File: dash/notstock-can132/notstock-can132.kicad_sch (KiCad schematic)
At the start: 28 parts, among them J1 OBD 12V GND H L, J2 wires from the display, U1 LMR16006YDDCR, U2 SN65HVD230

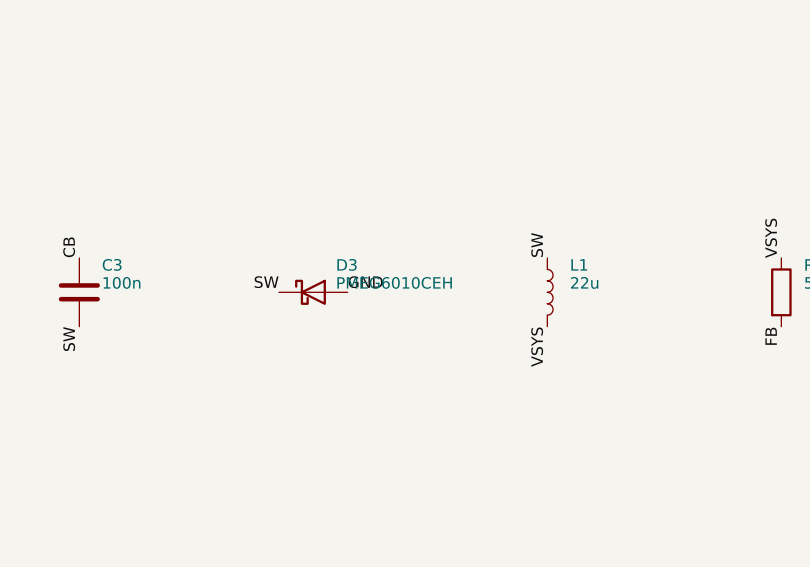
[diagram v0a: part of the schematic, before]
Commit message: CAN boards: D3 K16 (C2943756) for the PMEG6010CEH out of stock
Same footprint (SOD-123FL on the SOD-123F pads), 60 V 1 A Schottky.
BOM, schematic and the boards' LCSC fields updated on both boards.

Co-Authored-By: Claude Opus 5.5 <noreply@anthropic.com>
Claude-Session: https://claude.ai/code/session_018SKN4tJhAPpVCWtvRZgZpD
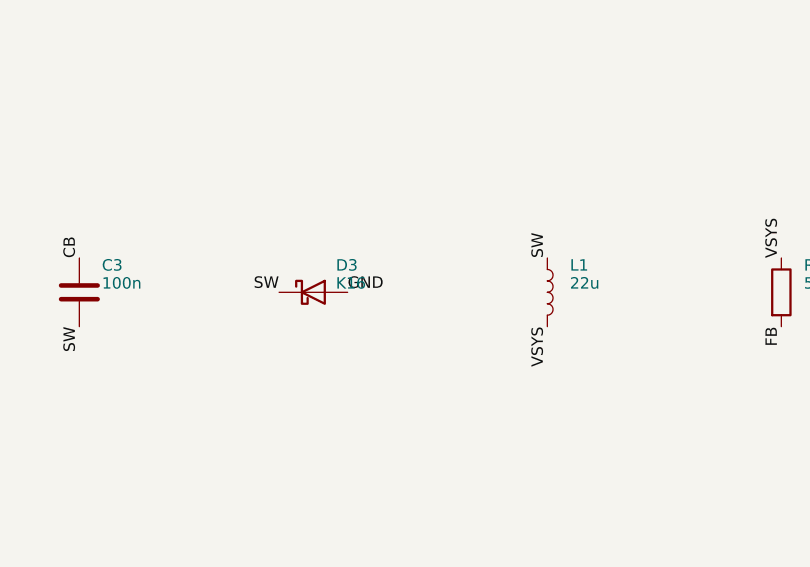
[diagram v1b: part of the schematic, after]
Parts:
- D3: value PMEG6010CEH -> K16; LCSC C110797 -> C2943756; MPN Nexperia PMEG6010CEH,115 -> GOODWORK K16 (60 V 1 A Schottky, SOD-123FL)
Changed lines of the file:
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@@
     (property "Reference" "D3" (at 129.5 137 0)
       (effects (font (size 1.27 1.27)) (justify left)))
-    (property "Value" "PMEG6010CEH" (at 129.5 139 0)
+    (property "Value" "K16" (at 129.5 139 0)
       (effects (font (size 1.27 1.27)) (justify left)))
     (property "Footprint" "Diode_SMD:D_SOD-123F" (at 127 140 0)
@@
     (property "Datasheet" "~" (at 127 140 0)
       (effects (font (size 1.27 1.27)) hide))
-    (property "LCSC" "C110797" (at 127 140 0)
+    (property "LCSC" "C2943756" (at 127 140 0)
       (effects (font (size 1.27 1.27)) hide))
-    (property "MPN" "Nexperia PMEG6010CEH,115" (at 127 140 0)
+    (property "MPN" "GOODWORK K16 (60 V 1 A Schottky, SOD-123FL)" (at 127 140 0)
       (effects (font (size 1.27 1.27)) hide))
     (pin "1")

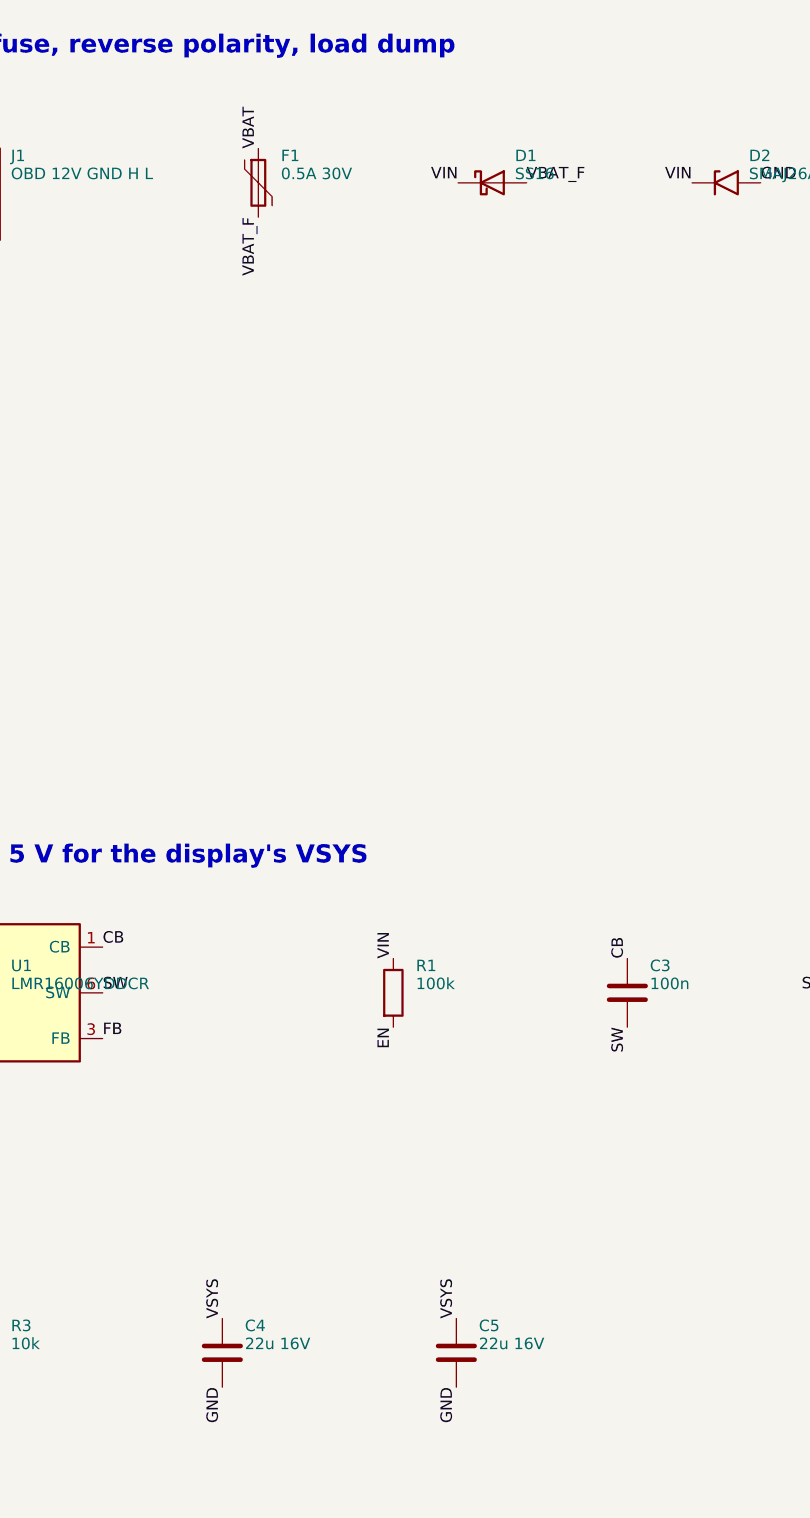
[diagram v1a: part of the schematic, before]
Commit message: CAN boards: JLCPCB basic parts where possible
D1 SS16 -> SS34 (C8678, basic, same SMA footprint) on both boards.
CAN 1.32: C4/C5 22 uF 1206 -> 0805 25 V (C45783, basic), rerouted,
DRC clean.

Co-Authored-By: Claude Opus 5.5 <noreply@anthropic.com>
Claude-Session: https://claude.ai/code/session_018SKN4tJhAPpVCWtvRZgZpD
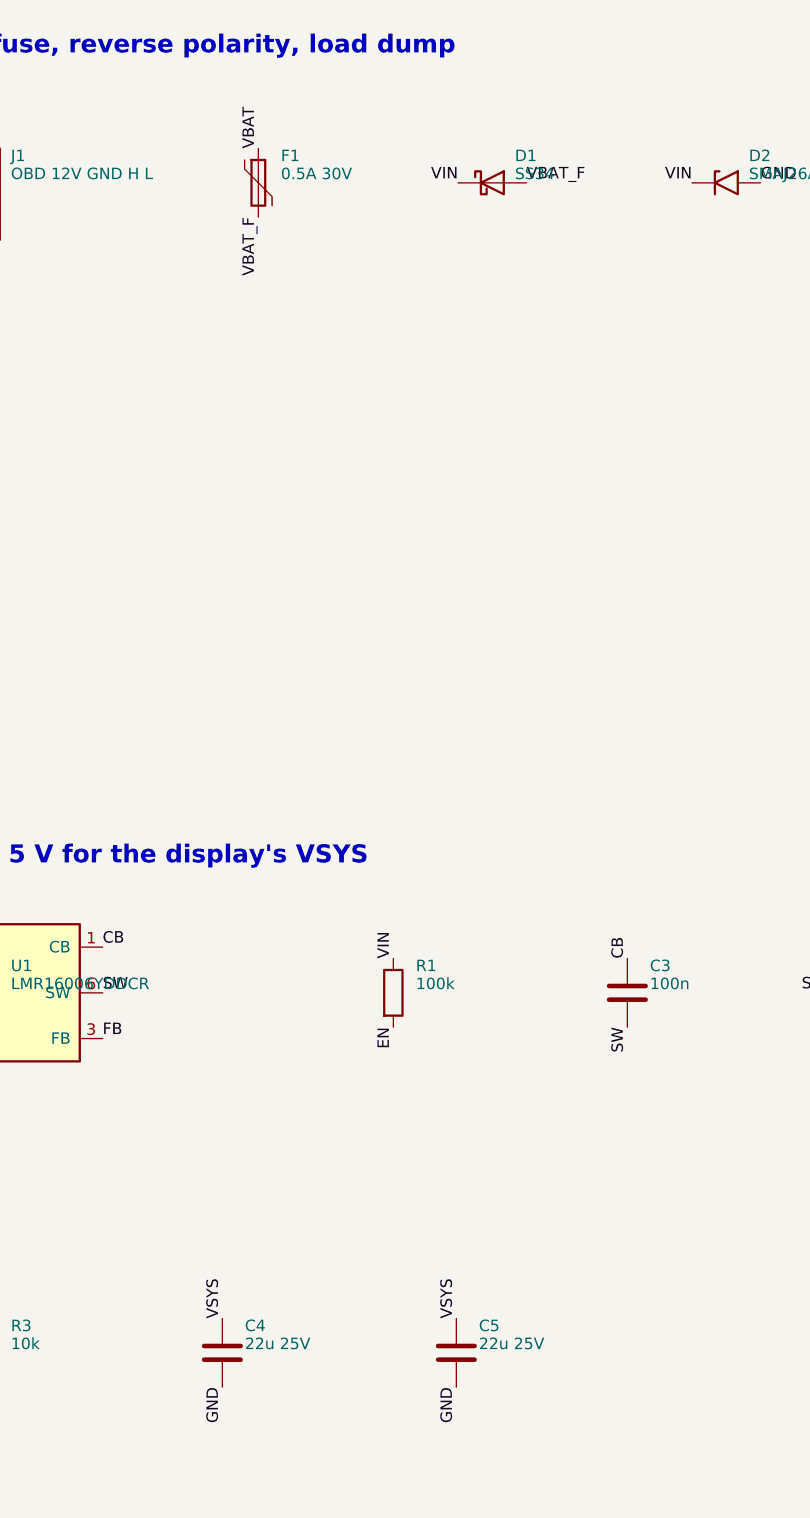
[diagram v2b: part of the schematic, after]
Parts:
- C4, C5: value 22u 16V -> 22u 25V; footprint Capacitor_SMD:C_1206_3216Metric -> Capacitor_SMD:C_0805_2012Metric; LCSC C90146 -> C45783; MPN Samsung CL31A226KOHNNNE (22 uF 16 V X5R 1206) -> Samsung CL21A226MAQNNNE (22 uF 25 V X5R 0805)
- D1: value SS16 -> SS34; LCSC C2758574 -> C8678; MPN UMW SS16 (60 V 1 A) -> MDD SS34 (40 V 3 A)
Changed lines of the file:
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@@
     (property "Reference" "D1" (at 88.5 47 0)
       (effects (font (size 1.27 1.27)) (justify left)))
-    (property "Value" "SS16" (at 88.5 49 0)
+    (property "Value" "SS34" (at 88.5 49 0)
       (effects (font (size 1.27 1.27)) (justify left)))
     (property "Footprint" "Diode_SMD:D_SMA" (at 86 50 0)
@@
     (property "Datasheet" "~" (at 86 50 0)
       (effects (font (size 1.27 1.27)) hide))
-    (property "LCSC" "C2758574" (at 86 50 0)
-      (effects (font (size 1.27 1.27)) hide))
-    (property "MPN" "UMW SS16 (60 V 1 A)" (at 86 50 0)
+    (property "LCSC" "C8678" (at 86 50 0)
+      (effects (font (size 1.27 1.27)) hide))
+    (property "MPN" "MDD SS34 (40 V 3 A)" (at 86 50 0)
       (effects (font (size 1.27 1.27)) hide))
     (pin "1")
@@
     (property "Reference" "C4" (at 58.5 177 0)
       (effects (font (size 1.27 1.27)) (justify left)))
-    (property "Value" "22u 16V" (at 58.5 179 0)
-      (effects (font (size 1.27 1.27)) (justify left)))
-    (property "Footprint" "Capacitor_SMD:C_1206_3216Metric" (at 56 180 0)
+    (property "Value" "22u 25V" (at 58.5 179 0)
+      (effects (font (size 1.27 1.27)) (justify left)))
+    (property "Footprint" "Capacitor_SMD:C_0805_2012Metric" (at 56 180 0)
       (effects (font (size 1.27 1.27)) hide))
     (property "Datasheet" "~" (at 56 180 0)
       (effects (font (size 1.27 1.27)) hide))
-    (property "LCSC" "C90146" (at 56 180 0)
-      (effects (font (size 1.27 1.27)) hide))
-    (property "MPN" "Samsung CL31A226KOHNNNE (22 uF 16 V X5R 1206)" (at 56 180 0)
+    (property "LCSC" "C45783" (at 56 180 0)
+      (effects (font (size 1.27 1.27)) hide))
+    (property "MPN" "Samsung CL21A226MAQNNNE (22 uF 25 V X5R 0805)" (at 56 180 0)
       (effects (font (size 1.27 1.27)) hide))
     (pin "1")
@@
     (property "Reference" "C5" (at 84.5 177 0)
       (effects (font (size 1.27 1.27)) (justify left)))
-    (property "Value" "22u 16V" (at 84.5 179 0)
-      (effects (font (size 1.27 1.27)) (justify left)))
-    (property "Footprint" "Capacitor_SMD:C_1206_3216Metric" (at 82 180 0)
+    (property "Value" "22u 25V" (at 84.5 179 0)
+      (effects (font (size 1.27 1.27)) (justify left)))
+    (property "Footprint" "Capacitor_SMD:C_0805_2012Metric" (at 82 180 0)
       (effects (font (size 1.27 1.27)) hide))
     (property "Datasheet" "~" (at 82 180 0)
       (effects (font (size 1.27 1.27)) hide))
-    (property "LCSC" "C90146" (at 82 180 0)
-      (effects (font (size 1.27 1.27)) hide))
-    (property "MPN" "Samsung CL31A226KOHNNNE (22 uF 16 V X5R 1206)" (at 82 180 0)
-      (effects (font (size 1.27 1.27)) hide))
-    (pin "1")
+    (property "LCSC" "C45783" (at 82 180 0)
+      (effects (font (size 1.27 1.27)) hide))
+    (property "MPN" "Samsung CL21A226MAQNNNE (22 uF 25 V X5R 0805)" (at 82 180 0)
+      (effects (font (size 1.27 1.27)) hide))
+    (pin "1")
